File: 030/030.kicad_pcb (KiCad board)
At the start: 2 copper layers, 18 x 21.6 mm, 5 parts, among them J1 030

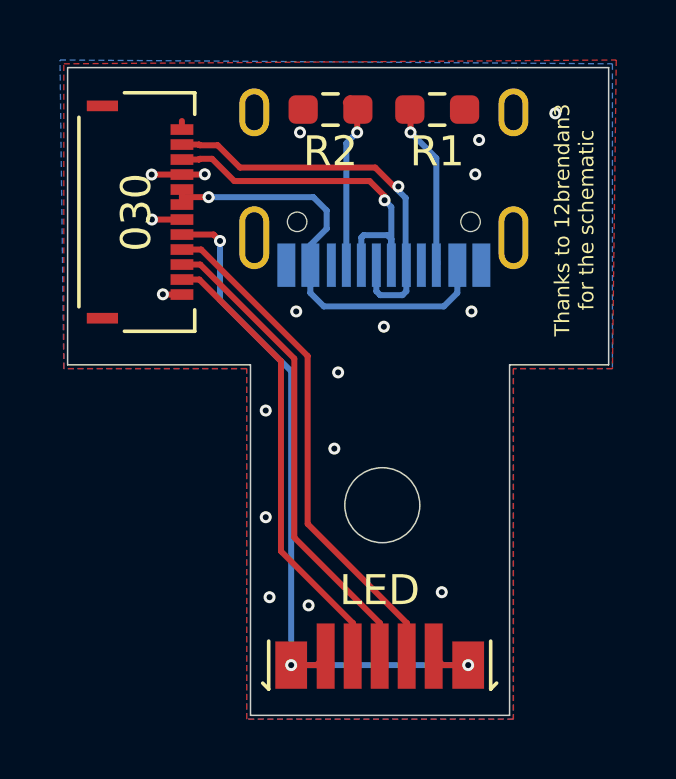
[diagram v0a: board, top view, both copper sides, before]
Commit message: Update 030 and 040 055 board to include screw mounting holes
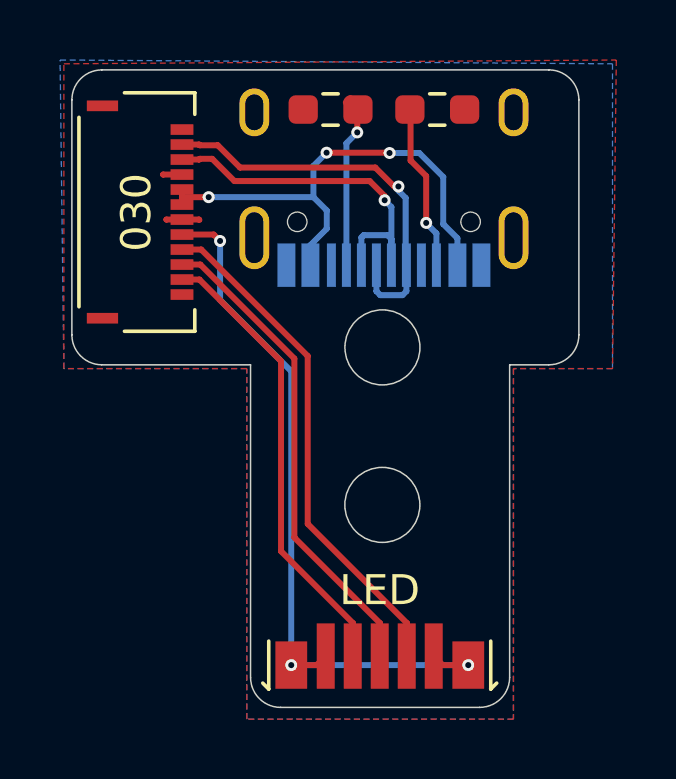
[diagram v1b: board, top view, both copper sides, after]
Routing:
- net GND: track 3.73 -> 1.77 mm, vias 18 -> 0
- net +5V: track 14.9 -> 16.8 mm, vias 1 -> 3
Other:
- board size 18 x 21.6 mm -> 16.9 x 21.3 mm
- net class Default removed
- board text removed: "Thanks to 12brendan3 for the schematic"
